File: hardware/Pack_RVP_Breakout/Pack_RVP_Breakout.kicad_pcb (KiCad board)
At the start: 2 copper layers, 33.5 x 21.6 mm, 5 parts, among them Q1 Q_PMOS_GDS, Q2 Q_PMOS_GDS

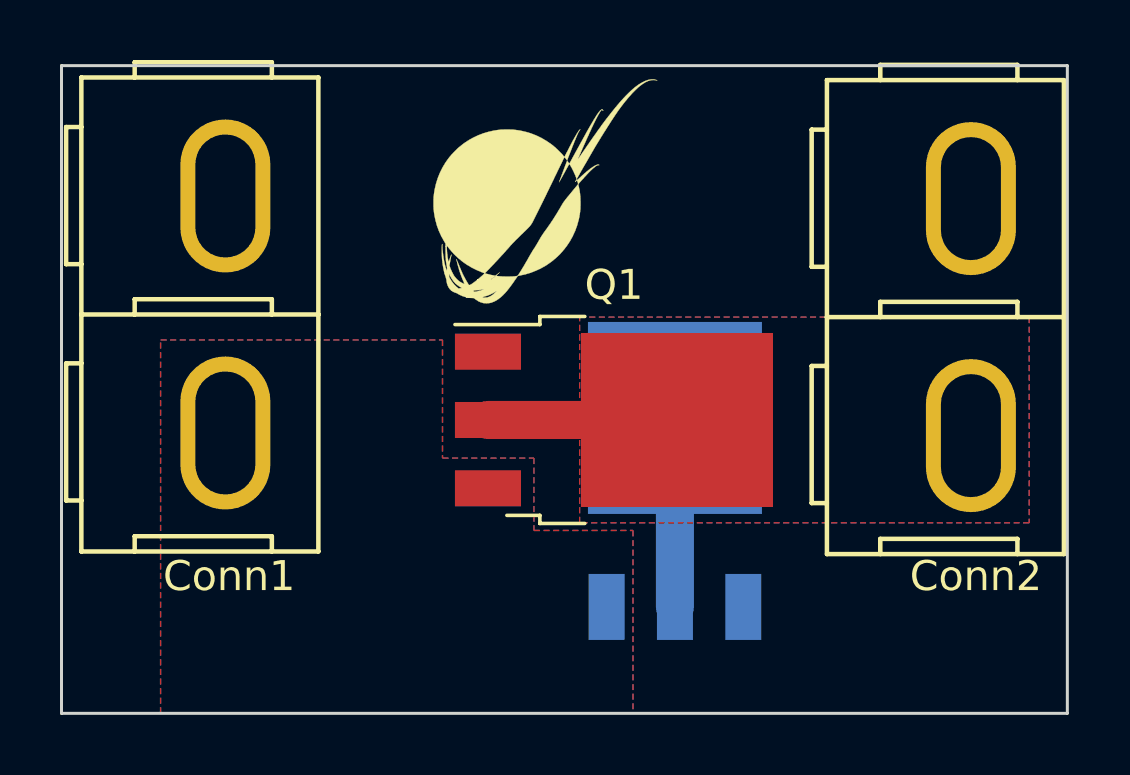
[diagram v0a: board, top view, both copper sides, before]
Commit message: Made 30V version
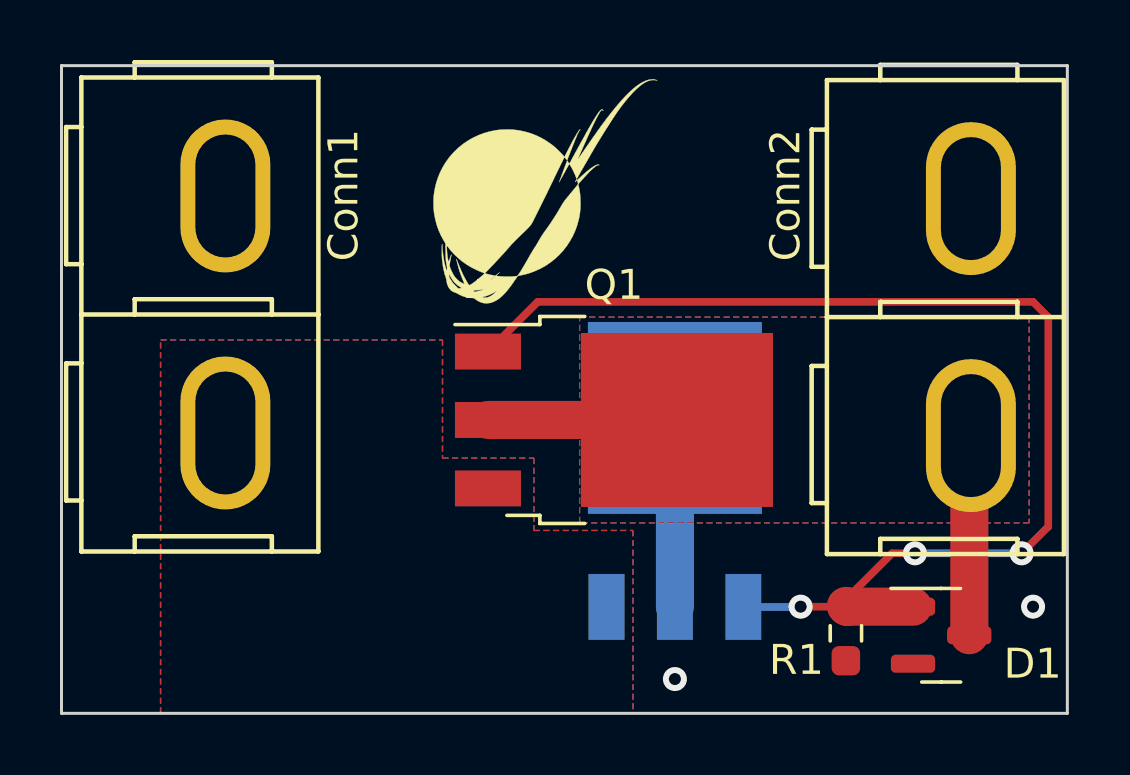
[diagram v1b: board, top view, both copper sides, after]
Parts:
- added D1: D_Zener, MRDT_Passives:SOT-23_Diode, F.Cu at (169.7, 75.0)
- added R1: 100k, Resistor_SMD:R_0603_1608Metric_Pad0.98x0.95mm_HandSolder, F.Cu at (165.8, 77.1)
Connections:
- Q1 pad 1: GND -> Net-(D1-Pad2)
- Q2 pad 1: GND -> Net-(D1-Pad2)
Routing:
- net Net-(D1-Pad2): track 0.00 -> 40.2 mm, vias 0 -> 3
- net +36V: track 12.6 -> 19.3 mm
- net GND: vias 0 -> 2
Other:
- board text added: "30V RVP Board, Rev1 Mars Rover Design Team Missouri S&T 2023 Grant Brinker"
- board text removed: "12V RVP Board, Rev1 Mars Rover Design Team Missouri S&T 2023 Grant Brinker"
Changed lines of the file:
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@@
   )
   (setup
+    (stackup
+      (layer "F.SilkS" (type "Top Silk Screen"))
+      (layer "F.Paste" (type "Top Solder Paste"))
+      (layer "F.Mask" (type "Top Solder Mask") (thickness 0.01))
+      (layer "F.Cu" (type "copper") (thickness 0.035))
+      (layer "dielectric 1" (type "core") (thickness 1.51) (material "FR4") (epsilon_r 4.5) (loss_tangent 0.02))
+      (layer "B.Cu" (type "copper") (thickness 0.035))
+      (layer "B.Mask" (type "Bottom Solder Mask") (thickness 0.01))
+      (layer "B.Paste" (type "Bottom Solder Paste"))
+      (layer "B.SilkS" (type "Bottom Silk Screen"))
+      (copper_finish "None")
+      (dielectric_constraints no)
+    )
     (pad_to_mask_clearance 0)
     (pcbplotparams
@@
   (net 2 "Net-(Conn1-Pad2)")
   (net 3 "+36V")
+  (net 4 "Net-(D1-Pad2)")
   (footprint "Package_TO_SOT_SMD:TO-252-3_TabPin2" (layer "F.Cu")
     (at 158.115 69.977)
@@
     (pad "" smd rect (at 0.425 -1.525) (size 3.05 2.75) (layers "F.Paste"))
     (pad "1" smd rect (at -4.2 -2.28) (size 2.2 1.2) (layers "F.Cu" "F.Paste" "F.Mask")
-      (net 1 "GND") (pinfunction "G") (pintype "input"))
+      (net 4 "Net-(D1-Pad2)") (pinfunction "G") (pintype "input"))
     (pad "2" smd rect (at -4.2 0) (size 2.2 1.2) (layers "F.Cu" "F.Paste" "F.Mask")
       (net 3 "+36V") (pinfunction "D") (pintype "passive"))
@@
       (net 2 "Net-(Conn1-Pad2)") (pinfunction "S") (pintype "passive"))
     (model "${KICAD6_3DMODEL_DIR}/Package_TO_SOT_SMD.3dshapes/TO-252-3_TabPin2.wrl"
+      (offset (xyz 0 0 0))
+      (scale (xyz 1 1 1))
+      (rotate (xyz 0 0 0))
+    )
+  )
+  (footprint "MRDT_Passives:SOT-23_Diode" (layer "F.Cu")
+    (at 169.672 75.0425)
+    (property "Sheetfile" "Pack_RVP_Breakout.kicad_sch")
+    (property "Sheetname" "")
+    (attr smd)
+    (fp_text reference "D1" (at 2.398 3.0625 unlocked) (layer "F.SilkS")
+      (effects (font (size 1 1) (thickness 0.15)))
+    )
+    (fp_text value "D_Zener" (at 0 1 unlocked) (layer "F.Fab")
+      (effects (font (size 1 1) (thickness 0.15)))
+    )
+    (fp_text user "${REFERENCE}" (at -0.65 2.11) (layer "F.Fab")
+      (effects (font (size 0.32 0.32) (thickness 0.05)))
+    )
+    (fp_text user "${REFERENCE}" (at 0 2.5 unlocked) (layer "F.Fab")
+      (effects (font (size 1 1) (thickness 0.15)))
+    )
+    (fp_line (start -0.65 0.55) (end -2.325 0.55) (layer "F.SilkS") (width 0.12))
+    (fp_line (start -0.65 3.67) (end -1.3 3.67) (layer "F.SilkS") (width 0.12))
+    (fp_line (start -0.65 0.55) (end 0 0.55) (layer "F.SilkS") (width 0.12))
+    (fp_line (start -0.65 3.67) (end 0 3.67) (layer "F.SilkS") (width 0.12))
+    (fp_line (start 1.27 0.41) (end -2.57 0.41) (layer "F.CrtYd") (width 0.05))
+    (fp_line (start -2.57 3.81) (end 1.27 3.81) (layer "F.CrtYd") (width 0.05))
+    (fp_line (start -2.57 0.41) (end -2.57 3.81) (layer "F.CrtYd") (width 0.05))
+    (fp_line (start 1.27 3.81) (end 1.27 0.41) (layer "F.CrtYd") (width 0.05))
+    (fp_line (start -0.975 0.66) (end 0 0.66) (layer "F.Fab") (width 0.1))
+    (fp_line (start -1.3 3.56) (end -1.3 0.985) (layer "F.Fab") (width 0.1))
+    (fp_line (start 0 0.66) (end 0 3.56) (layer "F.Fab") (width 0.1))
+    (fp_line (start -1.3 0.985) (end -0.975 0.66) (layer "F.Fab") (width 0.1))
+    (fp_line (start 0 3.56) (end -1.3 3.56) (layer "F.Fab") (width 0.1))
+    (pad "1" smd roundrect (at 0.2875 2.11) (size 1.475 0.6) (layers "F.Cu" "F.Paste" "F.Mask") (roundrect_rratio 0.25)
+      (net 3 "+36V") (pinfunction "K") (pintype "passive"))
+    (pad "2" smd roundrect (at -1.5875 1.16) (size 1.475 0.6) (layers "F.Cu" "F.Paste" "F.Mask") (roundrect_rratio 0.25)
+      (net 4 "Net-(D1-Pad2)") (pinfunction "A") (pintype "passive"))
+    (pad "3" smd roundrect (at -1.5875 3.06) (size 1.475 0.6) (layers "F.Cu" "F.Paste" "F.Mask") (roundrect_rratio 0.25))
+  )
+  (footprint "Resistor_SMD:R_0603_1608Metric_Pad0.98x0.95mm_HandSolder" (layer "F.Cu")
+    (at 165.847 77.089 -90)
+    (descr "Resistor SMD 0603 (1608 Metric), square (rectangular) end terminal, IPC_7351 nominal with elongated pad for handsoldering. (Body size source: IPC-SM-782 page 72, https://www.pcb-3d.com/wordpress/wp-content/uploads/ipc-sm-782a_amendment_1_and_2.pdf), generated with kicad-footprint-generator")
+    (tags "resistor handsolder")
+    (property "Sheetfile" "Pack_RVP_Breakout.kicad_sch")
+    (property "Sheetname" "")
+    (attr smd)
+    (fp_text reference "R1" (at 0.889 1.651 180) (layer "F.SilkS")
+      (effects (font (size 1 1) (thickness 0.15)))
+    )
+    (fp_text value "100k" (at 0 1.43 90) (layer "F.Fab")
+      (effects (font (size 1 1) (thickness 0.15)))
+    )
+    (fp_text user "${REFERENCE}" (at 0 0 90) (layer "F.Fab")
+      (effects (font (size 0.4 0.4) (thickness 0.06)))
+    )
+    (fp_line (start -0.254724 -0.5225) (end 0.254724 -0.5225) (layer "F.SilkS") (width 0.12))
+    (fp_line (start -0.254724 0.5225) (end 0.254724 0.5225) (layer "F.SilkS") (width 0.12))
+    (fp_line (start -1.65 -0.73) (end 1.65 -0.73) (layer "F.CrtYd") (width 0.05))
+    (fp_line (start -1.65 0.73) (end -1.65 -0.73) (layer "F.CrtYd") (width 0.05))
+    (fp_line (start 1.65 -0.73) (end 1.65 0.73) (layer "F.CrtYd") (width 0.05))
+    (fp_line (start 1.65 0.73) (end -1.65 0.73) (layer "F.CrtYd") (width 0.05))
+    (fp_line (start -0.8 -0.4125) (end 0.8 -0.4125) (layer "F.Fab") (width 0.1))
+    (fp_line (start 0.8 -0.4125) (end 0.8 0.4125) (layer "F.Fab") (width 0.1))
+    (fp_line (start -0.8 0.4125) (end -0.8 -0.4125) (layer "F.Fab") (width 0.1))
+    (fp_line (start 0.8 0.4125) (end -0.8 0.4125) (layer "F.Fab") (width 0.1))
+    (pad "1" smd roundrect (at -0.9125 0 270) (size 0.975 0.95) (layers "F.Cu" "F.Paste" "F.Mask") (roundrect_rratio 0.25)
+      (net 4 "Net-(D1-Pad2)") (pintype "passive"))
+    (pad "2" smd roundrect (at 0.9125 0 270) (size 0.975 0.95) (layers "F.Cu" "F.Paste" "F.Mask") (roundrect_rratio 0.25)
+      (net 1 "GND") (pintype "passive"))
+    (model "${KICAD6_3DMODEL_DIR}/Resistor_SMD.3dshapes/R_0603_1608Metric.wrl"
       (offset (xyz 0 0 0))
       (scale (xyz 1 1 1))
@@
     (property "Sheetname" "")
     (attr through_hole)
-    (fp_text reference "Conn1" (at 8.636 0) (layer "F.SilkS")
+    (fp_text reference "Conn1" (at -4.064 -3.81 90) (layer "F.SilkS")
       (effects (font (size 1 1) (thickness 0.15)))
     )
@@
     (property "Sheetname" "")
     (attr through_hole)
-    (fp_text reference "Conn2" (at 8.549 -0.04 180) (layer "F.SilkS")
+    (fp_text reference "Conn2" (at -4.151 6.31 -90) (layer "F.SilkS")
       (effects (font (size 1 1) (thickness 0.15)))
     )
@@
     (pad "" smd rect (at 3.775 -1.525 90) (size 3.05 2.75) (layers "B.Paste"))
     (pad "1" smd rect (at -4.2 2.28 90) (size 2.2 1.2) (layers "B.Cu" "B.Paste" "B.Mask")
-      (net 1 "GND") (pinfunction "G") (pintype "input"))
+      (net 4 "Net-(D1-Pad2)") (pinfunction "G") (pintype "input"))
     (pad "2" smd rect (at 2.1 0 90) (size 6.4 5.8) (layers "B.Cu" "B.Mask")
       (net 3 "+36V") (pinfunction "D") (pintype "passive"))
@@
     (effects (font (size 1 1) (thickness 0.15)) (justify mirror))
   )
-  (gr_text "12V RVP Board, Rev1\nMars Rover Design Team\nMissouri S&T 2023\nGrant Brinker" (at 156.718 61.595) (layer "B.SilkS")
+  (gr_text "30V RVP Board, Rev1\nMars Rover Design Team\nMissouri S&T 2023\nGrant Brinker" (at 156.718 61.595) (layer "B.SilkS")
     (effects (font (size 1 1) (thickness 0.15)) (justify mirror))
   )
@@
     (effects (font (size 1 1) (thickness 0.15)) (justify mirror))
   )
+  (via (at 160.147 78.613) (size 0.8) (drill 0.4) (layers "F.Cu" "B.Cu") (free) (net 1))
+  (via (at 172.085 76.2) (size 0.8) (drill 0.4) (layers "F.Cu" "B.Cu") (free) (net 1))
+  (segment (start 169.9595 70.5525) (end 170.014 70.498) (width 1.27) (layer "F.Cu") (net 3))
   (segment (start 153.915 69.977) (end 160.215 69.977) (width 1.27) (layer "F.Cu") (net 3))
+  (segment (start 169.9595 77.1525) (end 169.9595 70.5525) (width 1.27) (layer "F.Cu") (net 3))
   (segment (start 160.147 69.909) (end 160.147 76.209) (width 1.27) (layer "B.Cu") (net 3))
+  (segment (start 172.085 66.04) (end 172.593 66.548) (width 0.254) (layer "F.Cu") (net 4))
+  (segment (start 165.873 76.2025) (end 165.847 76.1765) (width 1.27) (layer "F.Cu") (net 4))
+  (segment (start 165.847 75.961) (end 165.847 76.1765) (width 0.254) (layer "F.Cu") (net 4))
+  (segment (start 167.386 74.422) (end 165.847 75.961) (width 0.254) (layer "F.Cu") (net 4))
+  (segment (start 155.575 66.04) (end 172.085 66.04) (width 0.254) (layer "F.Cu") (net 4))
+  (segment (start 164.338 76.2) (end 165.8235 76.2) (width 0.254) (layer "F.Cu") (net 4))
+  (segment (start 168.0845 76.2025) (end 165.873 76.2025) (width 1.27) (layer "F.Cu") (net 4))
+  (segment (start 153.918 67.697) (end 155.575 66.04) (width 0.254) (layer "F.Cu") (net 4))
+  (segment (start 168.148 74.422) (end 167.386 74.422) (width 0.254) (layer "F.Cu") (net 4))
+  (segment (start 172.593 73.533) (end 171.704 74.422) (width 0.254) (layer "F.Cu") (net 4))
+  (segment (start 153.915 67.697) (end 153.918 67.697) (width 0.254) (layer "F.Cu") (net 4))
+  (segment (start 165.8235 76.2) (end 165.847 76.1765) (width 0.254) (layer "F.Cu") (net 4))
+  (segment (start 172.593 66.548) (end 172.593 73.533) (width 0.254) (layer "F.Cu") (net 4))
+  (via (at 168.148 74.422) (size 0.8) (drill 0.4) (layers "F.Cu" "B.Cu") (net 4))
+  (via (at 164.338 76.2) (size 0.8) (drill 0.4) (layers "F.Cu" "B.Cu") (net 4))
+  (via (at 171.704 74.422) (size 0.8) (drill 0.4) (layers "F.Cu" "B.Cu") (net 4))
+  (segment (start 171.704 74.422) (end 168.148 74.422) (width 0.254) (layer "B.Cu") (net 4))
+  (segment (start 164.329 76.209) (end 164.338 76.2) (width 0.254) (layer "B.Cu") (net 4))
+  (segment (start 162.427 76.209) (end 164.329 76.209) (width 0.254) (layer "B.Cu") (net 4))
   (zone (net 3) (net_name "+36V") (layers F&B.Cu) (hatch edge 0.508)
     (priority 1)
